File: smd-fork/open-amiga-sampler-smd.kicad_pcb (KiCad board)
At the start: 2 copper layers, 36 x 21.1 mm, 18 parts, among them J1 Left, J2 Right, J3 DB25_Male, U1 ADC0820CCN, U2 MCP6001U

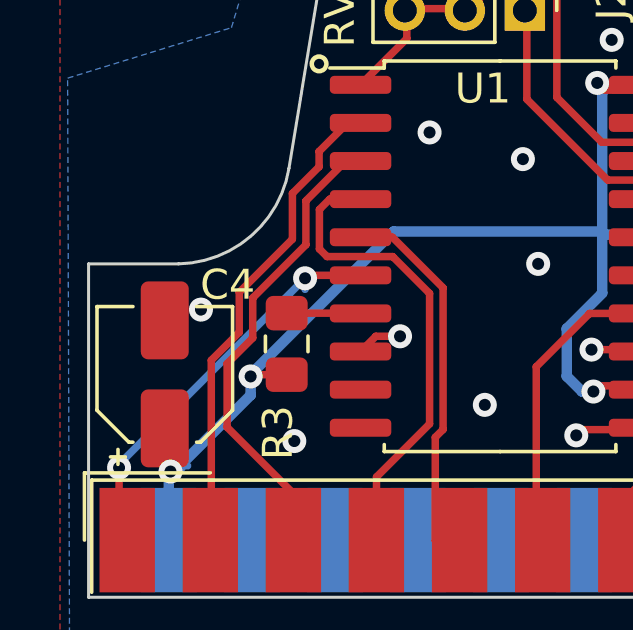
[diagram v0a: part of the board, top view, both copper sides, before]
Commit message: updates to case stls
minor PCB tweaks
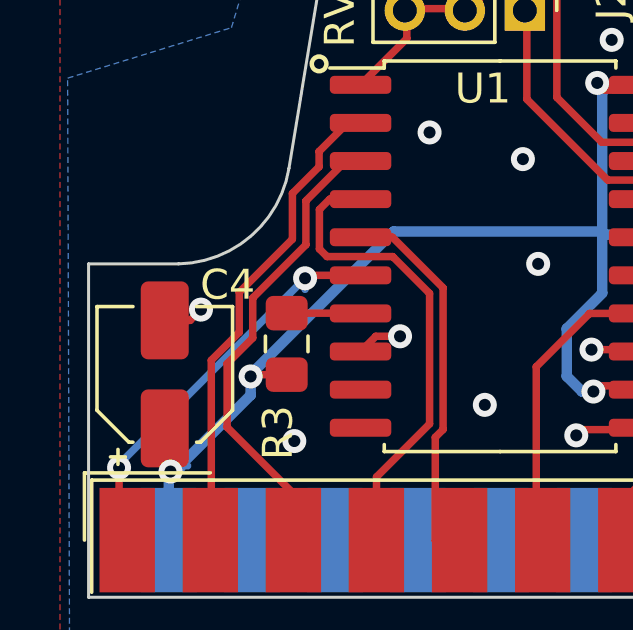
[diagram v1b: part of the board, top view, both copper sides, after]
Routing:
- net GND: track 12.3 -> 13.7 mm

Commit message: minor trace layout improvments
Rev 2
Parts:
- removed the REF** at (94.1, 140.3)
- added REF**: OSHW-Logo2_14.6x12mm_SilkScreen, Symbol:OSHW-Logo2_14.6x12mm_SilkScreen, B.Cu at (93.0, 139.6)
- moved R3 0.48 mm to (87.2, 142.9)
- moved U1 0.45 mm to (94.2, 140.0)
- moved C4 0.13 mm to (82.9, 143.4)
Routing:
- net VCC: track 60.6 -> 57.0 mm
- net D2: track 16.9 -> 14.8 mm
- net D7: track 14.9 -> 13.6 mm
- net D5: track 11.7 -> 12.9 mm
- net D1: track 16.5 -> 15.6 mm
- net GND: track 13.7 -> 12.9 mm
- net D6: track 12.2 -> 11.6 mm
- net D3: track 13.1 -> 12.6 mm
- net STROBE: track 14.6 -> 14.0 mm
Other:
- board text added: "Gain Adjust"
- board text added: "Rev 2"
- board text removed: "POT"

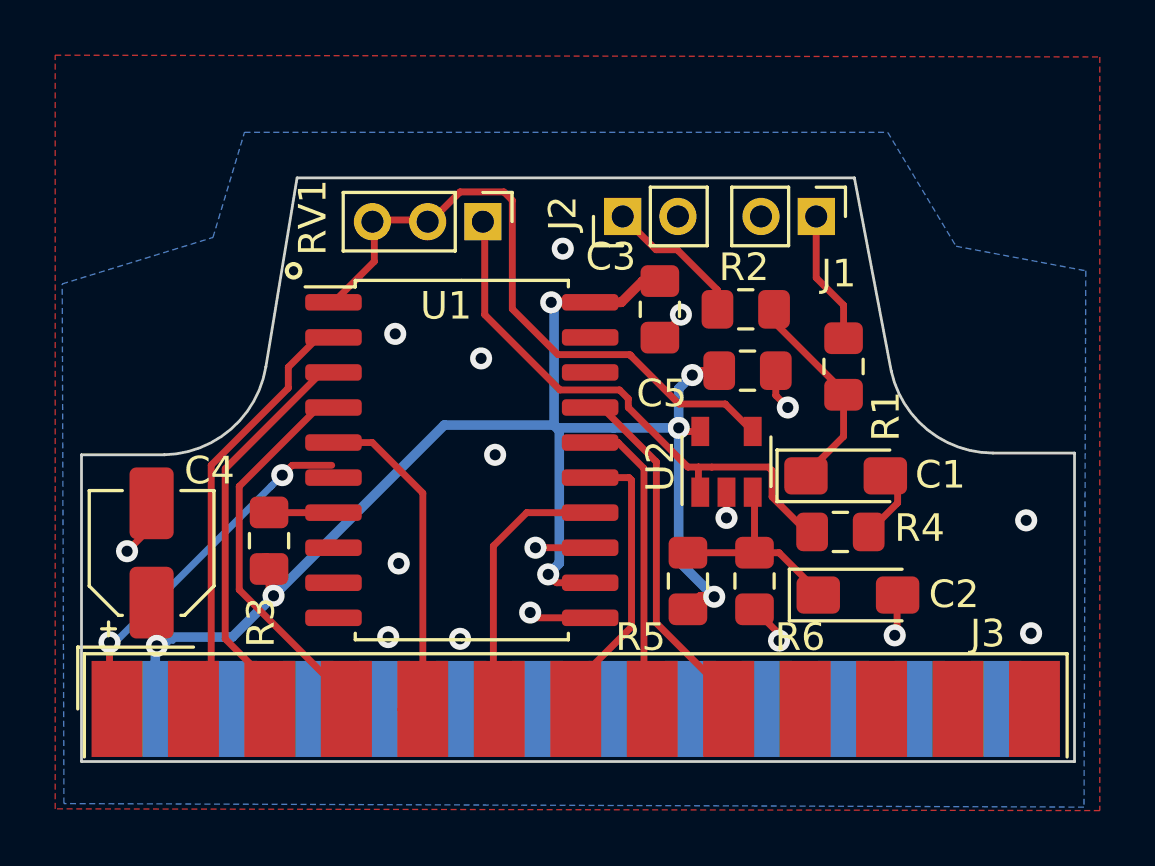
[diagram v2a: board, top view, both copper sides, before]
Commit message: rev 2
case files and board tweaks
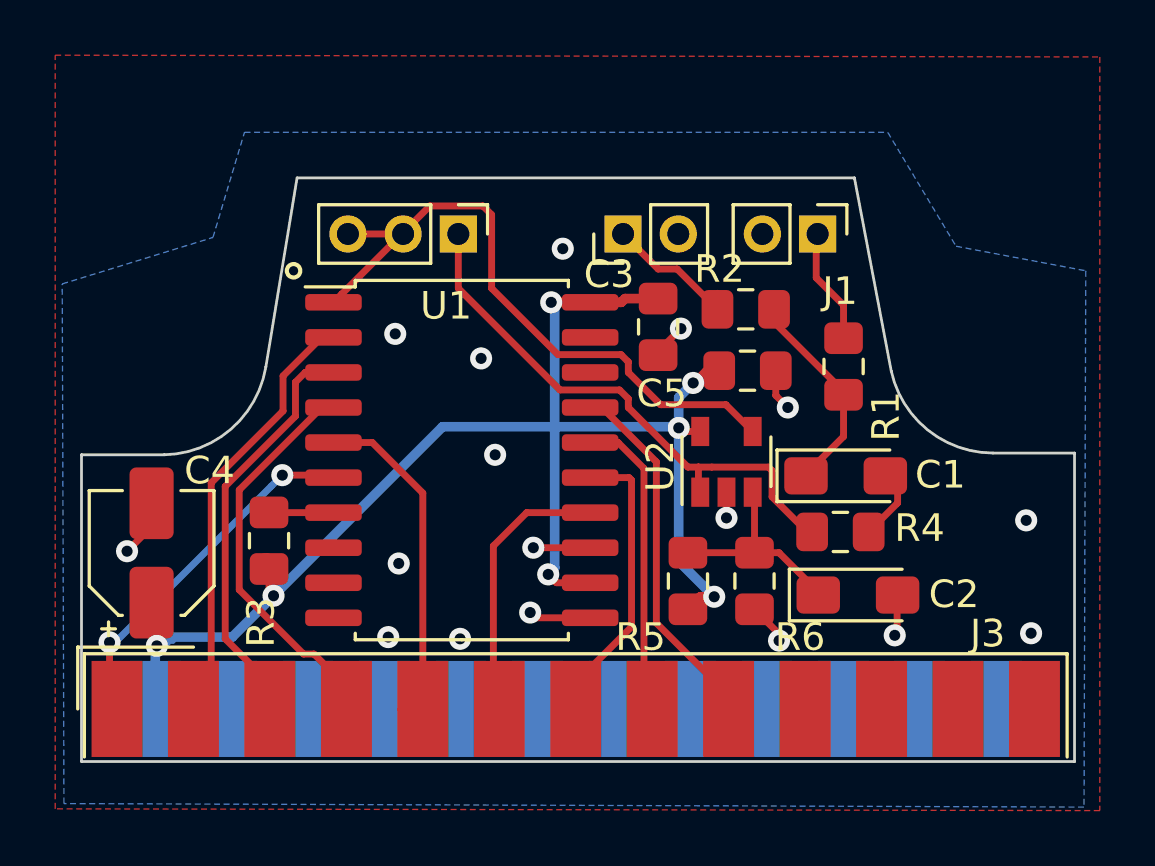
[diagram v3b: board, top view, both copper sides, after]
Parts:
- moved REF** 1.67 mm to (91.9, 140.9)
- moved RV1 0.99 mm to (94.0, 131.8)
- moved C3 0.64 mm to (101.3, 135.2)
- moved J1 0.64 mm to (107.1, 131.8)
- moved J2 0.64 mm to (100.0, 131.8)
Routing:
- net VCC: track 57.0 -> 55.5 mm
- net Net-(J2-Pad1): track 6.27 -> 5.13 mm
- net Net-(J1-Pad1): track 5.03 -> 4.21 mm
